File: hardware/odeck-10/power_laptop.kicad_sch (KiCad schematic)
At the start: 0 parts

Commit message: Draft power sheets (input, laptop output, rails) and BOM stock audit
- power_input: TPS26750/TPD4S480 EPR sink, LM74800 PD-in and barrel paths
  (reverse/OV/UV), hardware PD-in priority, EXT_PWR_PRESENT, INA237 VIN monitor
- power_laptop: LM51770 buck-boost 5-28 V x 5 A with VSEL-only voltage steps,
  gated source switch, interlocked bus-power sink, latched 30.8 V OVP, INA226
- power_rails: LM5148 5 V/8 A with ideal-diode backfeed blocking, TPS62933
  3.3 V and 1.15 V, INA226
- tools/bom_check.py: JLC-stock-only audit (>=5); all 116 parts pass
- schgen fixes: multi-line notes, PWR_FLAG skipped in verify, import --force
- docs: design notes per sheet, I2C map, cross-sheet integration items

Co-Authored-By: Claude Opus 5.5 <noreply@anthropic.com>
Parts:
- added C201, C202, C203, C204: 4.7u/100V, Capacitor_SMD:C_1210_3225Metric, symbol Device:C
- added C205: 47u/100V, Capacitor_SMD:CP_Elec_10x10, symbol Device:C_Polarized
- added C206, C207, C208, C209, C210, C211, C233: 10u/50V, Capacitor_SMD:C_1210_3225Metric, symbol Device:C
- added C212, C213: 100u/35V, Capacitor_SMD:CP_Elec_6.3x7.7, symbol Device:C_Polarized
- added C214, C220, C221, C228, C229, C234, C235, C236, C237: 100n/50V, Capacitor_SMD:C_0603_1608Metric, symbol Device:C
- added C215: 100n/100V, Capacitor_SMD:C_0603_1608Metric, symbol Device:C
- added C216: 1u/100V, Capacitor_SMD:C_0805_2012Metric, symbol Device:C
- added C217, C238: 1u/50V, Capacitor_SMD:C_0603_1608Metric, symbol Device:C
- added C218, C219: 22u, Capacitor_SMD:C_0805_2012Metric, symbol Device:C
- added C222: 100p, Capacitor_SMD:C_0402_1005Metric, symbol Device:C
- added C223: 22n, Capacitor_SMD:C_0402_1005Metric, symbol Device:C
- added C224: 6.8n, Capacitor_SMD:C_0402_1005Metric, symbol Device:C
- added C225: 82p, Capacitor_SMD:C_0402_1005Metric, symbol Device:C
- added C226, C240: 1n, Capacitor_SMD:C_0402_1005Metric, symbol Device:C
- added C227: 4.7u, Capacitor_SMD:C_0603_1608Metric, symbol Device:C
- added C230: 22n/50V, Capacitor_SMD:C_0603_1608Metric, symbol Device:C
- added C231, C232, C243: 100n, Capacitor_SMD:C_0402_1005Metric, symbol Device:C
- added C239: 3.3n, Capacitor_SMD:C_0402_1005Metric, symbol Device:C
- added C241: 10u, Capacitor_SMD:C_0805_2012Metric, symbol Device:C
- added C242: 470p, Capacitor_SMD:C_0402_1005Metric, symbol Device:C
- added D201: BZT52C5V1, Diode_SMD:D_SOD-123, symbol Device:D_Zener
- added D202: BAT54A, Package_TO_SOT_SMD:SOT-23, symbol Diode:BAT54A
- added D203: BAV70, Package_TO_SOT_SMD:SOT-23, symbol Diode:BAV70
- added D204: 1N4148W, Diode_SMD:D_SOD-123, symbol Device:D
- added L201: 10u, odeck:IND-SMD_L11.3-W10.0_XAL1010-332ME, symbol odeck:XAL1010-103MED
- added Q201, Q202: BSC0805LS, odeck:PG-TDSON-8_L5.2-W5.9-P1.27-LS6.2-BL-EP, symbol odeck:BSC0805LS
- added Q203, Q204, Q215: CSD18543Q3A, odeck:VSONP-8_L3.1-W3.1-P0.65-LS3.5-BL, symbol odeck:CSD18543Q3A
- added Q205, Q206, Q207, Q208, Q209, Q210, Q211, Q216, Q217, Q218: AO3400A, Package_TO_SOT_SMD:SOT-23, symbol Transistor_FET:AO3400A
- added Q212: 2N7002, Package_TO_SOT_SMD:SOT-23, symbol Transistor_FET:2N7002
- added Q213, Q214: BSC040N08NS5, odeck:PG-TDSON-8_L5.9-W5.1-P1.27-LS6.2-BL, symbol odeck:BSC040N08NS5
- added R201: 4m, Resistor_SMD:R_2512_6332Metric, symbol Device:R
- added R202: 8m, Resistor_SMD:R_2512_6332Metric, symbol Device:R
- added R203, R204, R205, R206, R217, R218: 0, Resistor_SMD:R_0402_1005Metric, symbol Device:R
- added R207: 200k, Resistor_SMD:R_0805_2012Metric, symbol Device:R
- added R208: 43k, Resistor_SMD:R_0402_1005Metric, symbol Device:R
- added R209: 10, Resistor_SMD:R_0603_1608Metric, symbol Device:R
- added R210, R211: 10, Resistor_SMD:R_0402_1005Metric, symbol Device:R
- added R212: 86.6k, Resistor_SMD:R_0402_1005Metric, symbol Device:R
- added R213, R220, R225, R228, R231, R232, R238, R240, R243: 100k, Resistor_SMD:R_0402_1005Metric, symbol Device:R
- added R214: 6.49k, Resistor_SMD:R_0402_1005Metric, symbol Device:R
- added R215: 62k, Resistor_SMD:R_0402_1005Metric, symbol Device:R
- added R216, R219, R236, R239, R247, R249, R253, R255: 10k, Resistor_SMD:R_0402_1005Metric, symbol Device:R
- added R221, R223: 24.3k, Resistor_SMD:R_0402_1005Metric, symbol Device:R
- added R222: 1.5k, Resistor_SMD:R_0402_1005Metric, symbol Device:R
- added R224, R227, R230, R248: 1k, Resistor_SMD:R_0402_1005Metric, symbol Device:R
- added R226: 8.66k, Resistor_SMD:R_0402_1005Metric, symbol Device:R
- added R229: 5.23k, Resistor_SMD:R_0402_1005Metric, symbol Device:R
- added R233: 470k, Resistor_SMD:R_0805_2012Metric, symbol Device:R
- added R234: 150, Resistor_SMD:R_2512_6332Metric, symbol Device:R
- added R235: 255k, Resistor_SMD:R_0402_1005Metric, symbol Device:R
- added R237: 100, Resistor_SMD:R_0402_1005Metric, symbol Device:R
- added R241: 5m, Resistor_SMD:R_2512_6332Metric, symbol Device:R
- added R242: 422k, Resistor_SMD:R_0402_1005Metric, symbol Device:R
- added R244: 121k, Resistor_SMD:R_0402_1005Metric, symbol Device:R
- added R245, R250, R252: 47k, Resistor_SMD:R_0402_1005Metric, symbol Device:R
- added R246: 40.2k, Resistor_SMD:R_0402_1005Metric, symbol Device:R
- added R251: 1.1M, Resistor_SMD:R_0402_1005Metric, symbol Device:R
- added R254: 4.7k, Resistor_SMD:R_0402_1005Metric, symbol Device:R
- added U201: LM51770, odeck:HTSSOP-38_L9.7-W4.4-P0.50-LS6.4-BL-EP, symbol odeck:LM51770DCPR
- added U202: LM74800-Q1, odeck:WSON-12_L3.0-W3.0-P0.50-TL-EP-2, symbol odeck:LM74800QDRRRQ1
- added U203: SN74LVC1G11, Package_TO_SOT_SMD:SOT-23-6, symbol 74xGxx:74LVC1G11
- added U204: INA226, odeck:MSOP-10_L3.0-W3.0-P0.50-LS5.0-BL, symbol odeck:INA226AIDGSR
- added U205: LM74502, odeck:SOT-23-8_L2.9-W1.6-P0.65-LS2.8-BL, symbol odeck:LM74502DDFR
- added U206: TPS259470A, odeck:VQFN-10_L2.0-W2.0-P0.45-TL, symbol odeck:TPS259470ARPWR
- added U207: TLV3011, odeck:SOT-23-6_L2.9-W1.6-P0.95-LS2.8-BR, symbol odeck:TLV3011AIDBVR
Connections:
- new net +3V3: C231.1, C232.1, C243.1, R219.2, R239.2, R255.2, U203.5 (VCC), U204.1 (A1), U204.6 (VS+), U207.6 (VCC)
- new net +5V: C241.1, U206.6 (OUT)
- new net BB_BIAS: C217.1, R209.2, U201.1 (BIAS)
- new net BB_CFG: R214.1, U201.13 (CFG)
- new net BB_COMP: C225.1, R215.1, U201.18 (COMP)
- new net BB_COMPZ: C224.1, R215.2
- new net BB_CSA: C222.1, R210.2, U201.37 (CSA)
- new net BB_CSB: C222.2, R211.2, U201.38 (CSB)
- new net BB_DIS: Q212.3 (D), R234.2
- new net BB_EN: Q209.3 (D), R207.2, R208.1, U201.4 (EN/UVLO)
- new net BB_ENKILL: D201.1 (K), Q208.1 (G), Q209.1 (G), Q210.3 (D), Q212.1 (G), R233.2
- new net BB_ENS: Q210.2 (S), Q211.3 (D)
- new net BB_FB: R220.2, R221.1, R222.1, U201.19 (FB)
- new net BB_FBM: C227.1, R222.2, R223.1, R226.1, R229.1
- new net BB_G1: Q201.4 (G), R203.2
- new net BB_G2: Q202.4 (G), R204.2
- new net BB_G3: Q203.4 (G), R205.2
- new net BB_G4: Q204.4 (G), R206.2
- new net BB_HB1: C220.1, U201.35 (HB1)
- new net BB_HB2: C221.1, U201.26 (HB2)
- new net BB_HO1: R203.1, U201.34 (HO1)
- new net BB_HO2: R206.1, U201.27 (HO2)
- new net BB_IMON: R216.1, U201.6 (IMONOUT)
- new net BB_IMONZ: C226.1, R216.2
- new net BB_LO1: R204.1, U201.32 (LO1)
- new net BB_LO2: R205.1, U201.29 (LO2)
- new net BB_LS: L201.1, R201.2, R211.1
- new net BB_MODE: R217.1, R218.1, U201.12 (MODE)
- new net BB_PSO: C206.1, C207.1, C208.1, C209.1, Q204.5 (D), Q204.6 (D), Q204.7 (D), Q204.8 (D), Q204.9 (D), R202.1, U201.23 (ISNSP)
- new net BB_RT: R212.1, U201.15 (RT)
- new net BB_SLOPE: R213.1, U201.14 (SLOPE)
- new net BB_SS: C223.1, U201.16 (SS/ATRK)
- new net BB_SW1: C220.2, Q201.1 (S), Q201.2 (S), Q201.3 (S), Q202.5 (D), Q202.6 (D), Q202.7 (D), Q202.8 (D), Q202.9 (EP), R201.1, R210.1, U201.36 (SW1)
- new net BB_SW2: C221.2, L201.2, Q203.5 (D), Q203.6 (D), Q203.7 (D), Q203.8 (D), Q203.9 (D), Q204.1 (S), Q204.2 (S), Q204.3 (S), U201.25 (SW2)
- new net BB_VCC: C218.1, C219.1, R218.2, U201.11 (SYNC), U201.31 (VCC)
- new net BB_VS0D: Q205.3 (D), R223.2
- new net BB_VS0G: Q205.1 (G), R224.2
- new net BB_VS1D: Q206.3 (D), R226.2
- new net BB_VS1G: Q206.1 (G), R227.2
- new net BB_VS2D: Q207.3 (D), R229.2
- new net BB_VS2G: Q207.1 (G), R230.2
- new net EXT_PWR_PRESENT: Q216.1 (G), U203.3
- new net GND: C201.2, C202.2, C203.2, C204.2, C205.2, C206.2, C207.2, C208.2, C209.2, C210.2, C211.2, C212.2, C213.2, C214.2, C215.2, C216.2, C217.2, C218.2, C219.2, C223.2, C224.2, C225.2, C226.2, C227.2, C228.2, C230.2, C231.2, C232.2, C233.2, C234.2, C235.2, C236.2, C238.2, C239.2, C240.2, C241.2, C242.2, C243.2, D201.2 (A), Q202.1 (S), Q202.2 (S), Q202.3 (S), Q203.1 (S), Q203.2 (S), Q203.3 (S), Q205.2 (S), Q206.2 (S), Q207.2 (S), Q208.2 (S), Q209.2 (S), Q211.2 (S), Q212.2 (S), Q216.2 (S), Q217.2 (S), Q218.2 (S), R208.2, R212.2, R213.2, R214.2, R217.2, R221.2, R225.2, R228.2, R231.2, R232.2, R236.2, R238.2, R240.2, R243.2, R245.2, R247.2, R248.2, R250.2, R252.2, U201.10 (DTRK), U201.17 (AGND), U201.30 (PGND), U201.39 (EP), U202.7 (GND), U203.2 (GND), U204.2 (A0), U204.7 (GND), U205.2 (GND), U206.8 (GND), U207.2 (GND)
- new net I2C_SYS_SCL: U204.5 (SCL)
- new net I2C_SYS_SDA: U204.4 (SDA)
- new net LAPTOP_OVP_N: D202.2, Q211.1 (G), Q218.3 (D), R255.1
- new net LAPTOP_SNK_EN: R249.1
- new net LAPTOP_SRC_EN: R240.1, U203.1
- new net OVP_DIV: C242.1, R251.2, R252.1, R254.2, U207.3 (IN+)
- new net OVP_FB: D204.1 (K), R254.1
- new net OVP_REF: U207.4 (IN-), U207.5 (REF)
- new net OVP_TOP: D203.3 (K), R251.1
- new net OVP_TRIP: D204.2 (A), Q218.1 (G), R253.1, U207.1 (OUT)
- new net SNK_DVDT: C239.1, U206.7 (DVDT)
- new net SNK_GATE: Q215.4 (G), U205.6 (GATE)
- new net SNK_ILM: R248.1, U206.9 (ILM)
- new net SNK_ITIMER: C240.1, U206.10 (ITIMER)
- new net SNK_MID: C238.1, Q215.1 (S), Q215.2 (S), Q215.3 (S), R244.1, R246.1, U205.8 (SRC), U206.5 (IN)
- new net SNK_ON: Q216.3 (D), Q217.3 (D), R249.2, R250.1, U205.1 (EN/UVLO)
- new net SNK_OV: R242.2, R243.1, U205.7 (OV)
- new net SNK_OVLO: R246.2, R247.1, U206.2 (OVLO/OVCSEL)
- new net SNK_UV: R244.2, R245.1, U206.1 (EN/UVLO)
- new net SNK_VCAP: C237.1, U205.4 (VCAP)
- new net SRC_CAP: C229.1, U202.11 (CAP)
- new net SRC_DGATE: Q213.4 (G), U202.1 (DGATE)
- new net SRC_DVDT: C230.1, R237.2
- new net SRC_HGATE: Q214.4 (G), R237.1, U202.8 (HGATE)
- new net SRC_MID: C228.1, C229.2, Q213.5 (D), Q213.6 (D), Q213.7 (D), Q213.8 (D), Q214.5 (D), Q214.6 (D), Q214.7 (D), Q214.8 (D), U202.10 (VS), U202.12 (C)
- new net SRC_ON: Q217.1 (G), R238.1, U202.6 (EN/UVLO), U203.4
- new net SRC_OV: R235.2, R236.1, U202.5 (OV)
- new net SRC_OVT: R235.1, U202.4 (SW)
- new net SRC_PGOK: D202.3, R239.1, U203.6
- new net VBB_EN: Q210.1 (G), R232.1, R253.2
- new net VBB_OUT: C210.1, C211.1, C212.1, C213.1, C214.1, D203.2 (A), Q213.1 (S), Q213.2 (S), Q213.3 (S), R202.2, R209.1, R220.1, R234.1, U201.20 (VOUT), U201.22 (ISNSN), U202.2 (A)
- new net VBB_PG: D202.1, Q208.3 (D), R219.1, U201.7 (nFLT)
- new net VBB_VSEL0: R224.1, R225.1
- new net VBB_VSEL1: R227.1, R228.1
- new net VBB_VSEL2: R230.1, R231.1
- new net VBUS_LAPTOP: C233.1, C234.1, D203.1 (A), R241.2, U202.3 (VSNS), U204.8 (VBUS), U204.9 (VIN-)
- new net VBUS_LSW: C235.1, C236.1, C237.2, Q214.1 (S), Q214.2 (S), Q214.3 (S), Q215.5 (D), Q215.6 (D), Q215.7 (D), Q215.8 (D), Q215.9 (D), R241.1, R242.1, U202.9 (OUT), U204.10 (VIN+), U205.5 (VS)
- new net VIN: C201.1, C202.1, C203.1, C204.1, C205.1, C215.1, C216.1, Q201.5 (D), Q201.6 (D), Q201.7 (D), Q201.8 (D), Q201.9 (EP), R207.1, R233.1, U201.3 (VIN)
- no-connect marks 0 -> 13
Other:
- note added: "1. LM51770 4-SWITCH BUCK-BOOST POWER STAGE VIN 9-50 V -> VBB_OUT 5.1/9/15/20/28 V, 5 A (140 W) fsw = 347 kHz (RT 86.6k). L = Coilcraft XAL1010-103 10 uH (Isat 17.5 A, 14.75 mOhm max). Ripple: 3.4 A p-p worst (48 V -> 28 V buck), 2.0 A (14 V -> 28 V boost). Input half-bridge: 2x BSC0805LS (100 V, 7.7 mOhm @4.5 V, Qg 16 nC). Output: 2x CSD18543Q3A (60 V, 12 mOhm). Peak current sense RCS = 4 mOhm (W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"
- note added: "2. LM51770 CONTROLLER BIAS from VBB_OUT (10 R/1 uF): VCC LDO runs from min(VIN, VBB_OUT) above 6.5 V -> less LDO loss at 48 V in. EN/UVLO: 200k/43k from VIN -> on at 8.1 V, off at 6.8 V (5 uA hysteresis current). Q pulls EN/UVLO low unless VBB_EN AND LAPTOP_OVP_N (see section 3). CFG 6.49k = R2D #7: spread spectrum ON, hiccup ON, PSM entry 10 %, average current LIMIT on ISNS. SYNC = VCC (positive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"
- note added: "3. OUTPUT VOLTAGE SELECT (PMG1 GPIOs only; RP2350 has no path here) VOUT = 1 V x (1 + Rtop x Gfb). Rtop 100k, Rbot 24.3k -> 5.115 V with all VSEL low (default, no firmware). Switched branches hang off node BB_FBM, which connects to FB through Rs = 1.5k and is held by Cm = 4.7 uF: any VSEL change (even several bits at once) moves the FB current as ONE first-order exponential, tau = Cm x (Rs || bra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"
- note added: "4. LAPTOP SOURCE SWITCH VBB_OUT -> VBUS_LSW -> 5 mOhm -> VBUS_LAPTOP LM74800-Q1: Q (DGATE) = ideal diode (blocks laptop -> VBB_OUT in < 1 us), Q (HGATE) = on/off, common drain, 2x BSC040N08NS5 (80 V, 4 mOhm @10 V): 5 A -> 0.26 W total. HARDWARE ENABLE: SRC_ON = LAPTOP_SRC_EN AND EXT_PWR_PRESENT AND (VBB_PG AND LAPTOP_OVP_N) 74LVC1G11 3-input AND; VBB_PG and LAPTOP_OVP_N (both open-drain, 10k pull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"
- note added: "5. VBUS_LAPTOP MONITOR + CAPACITANCE INA226 on I2C_SYS at 0x44 (A1 = VS, A0 = GND). Shunt 5 mOhm (WSL2512): 5 A -> 25 mV of +-81.92 mV, 0.125 W. Bidirectional: + = sourcing to laptop, - = bus-powered sink. CURRENT_LSB 0.5 mA -> CAL = 2048. VBUS pin on the connector side (36 V max > 32.6 V backstop). Kelvin-route IN+/IN-. ALERT unused. Capacitance on the connector side (VBUS_LAPTOP + VBUS_LSW, no 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"
- note added: "6. BUS-POWER SINK SWITCH VBUS_LSW -> SNK_MID -> +5V (only without external power) Stage 1, 60 V blocking: CSD18543Q3A driven by LM74502 (charge pump, 3.2-65 V). Off -> blocks up to 60 V (VBUS is 28 V when we source); body diode points back to VBUS, reverse handled by stage 2. OV cut-off 422k/100k -> 6.5 V (6.1-6.9 V), 1 us: a >5 V contract can never reach +5V. Stage 2, TPS259470A eFuse (28 V abs)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"
- note added: "7. INDEPENDENT VBUS OVP (latched) -> LAPTOP_OVP_N Senses max(VBUS_LAPTOP, VBB_OUT) through BAV70 (100 V): also catches a run-away buck-boost before the source switch closes. 1.1M/47k + 0.45 V diode: trip = 1.242 x 24.4 + 0.45 = 30.8 V (29.6-32.0 V incl. 1 % ref, 15 mV offset, 1 % R) > 28.7 V max regulation; 470 pF -> 21 us filter. TLV3011 (open-drain, internal 1.242 V ref): output pulled up to VB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"
- note removed: "TODO — planned contents: LM51770 buck-boost 9-48V -> 5/9/15/20/28V x5A, voltage steps via PMG1 GPIO feedback switching, back-to-back source switch to laptop VBUS (enable = ext power AND PG), independent hardware OVP (~30V)."
- title: odeck-10 — Laptop power out -> odeck-10 — Laptop power (buck-boost, source/sink switches, OVP)

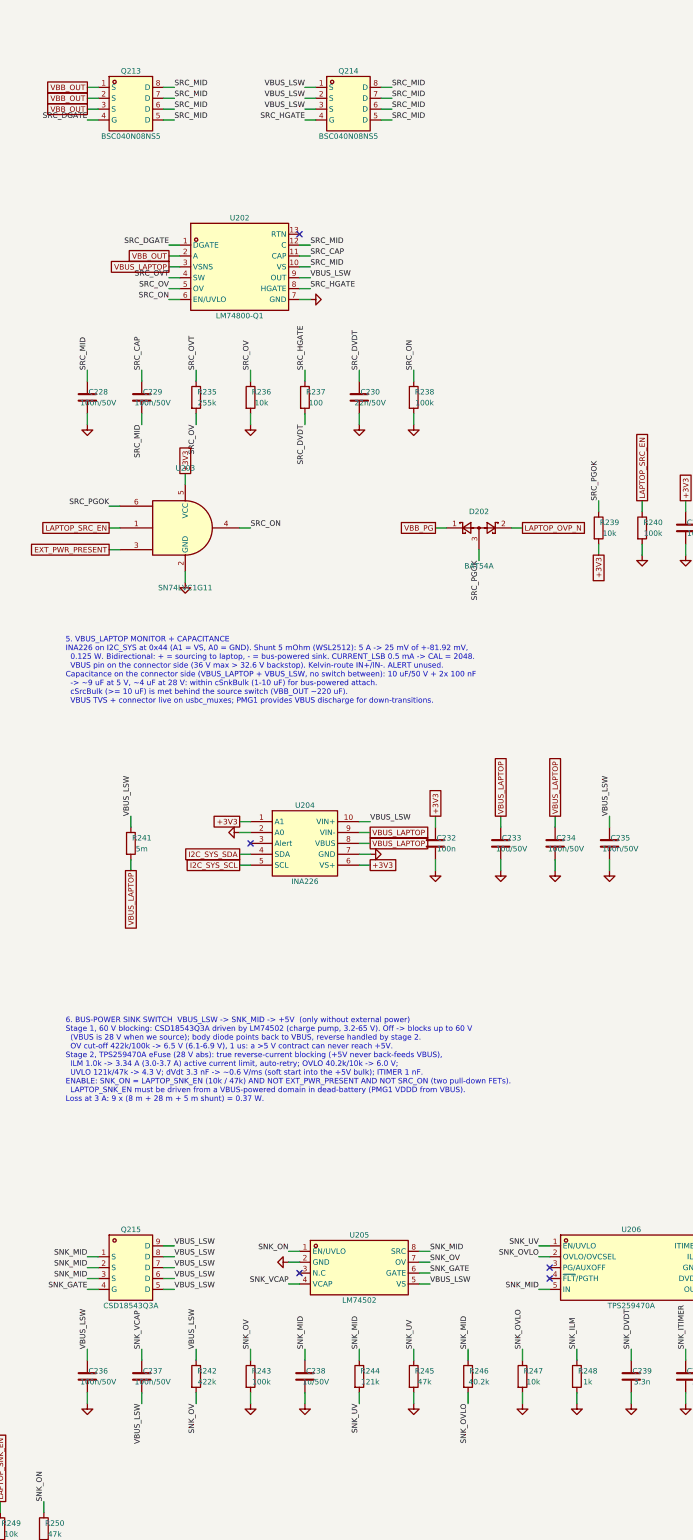
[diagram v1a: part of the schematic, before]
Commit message: Draft data-path sheets: PD controller, USB-C muxes/DP, USB hub
- pd_pmg1: PMG1-S3 (CYPM1321, dead-battery Rd) dual-port: laptop EPR source +
  DP UFP_D, downstream 5 V/3 A + DP DFP_D, HPD relay, VBUS-powered cold start,
  I2C 0x42, SWD/reset via cuttable jumpers
- usbc_muxes: laptop + downstream USB-C, TUSB1064/TUSB1046 in GPIO mode,
  TPD4S480 (EPR) / TPD6S300 CC protection, 10G-rated ESD, AC coupling
- usb_hub: USB7206C port map, SMBus-optional boot, reset gated by RAILS_PG,
  BC1.2 on USB-A ports, hub-TX AC caps
- schgen: in_bom option; nets: VBUS_LSW, PMG1_VDDD, hub/mux/CC links
- import_lcsc.sh: guard against overwriting other parts' footprints
- 137 parts, all JLC stock >= 5

Co-Authored-By: Claude Opus 5.5 <noreply@anthropic.com>
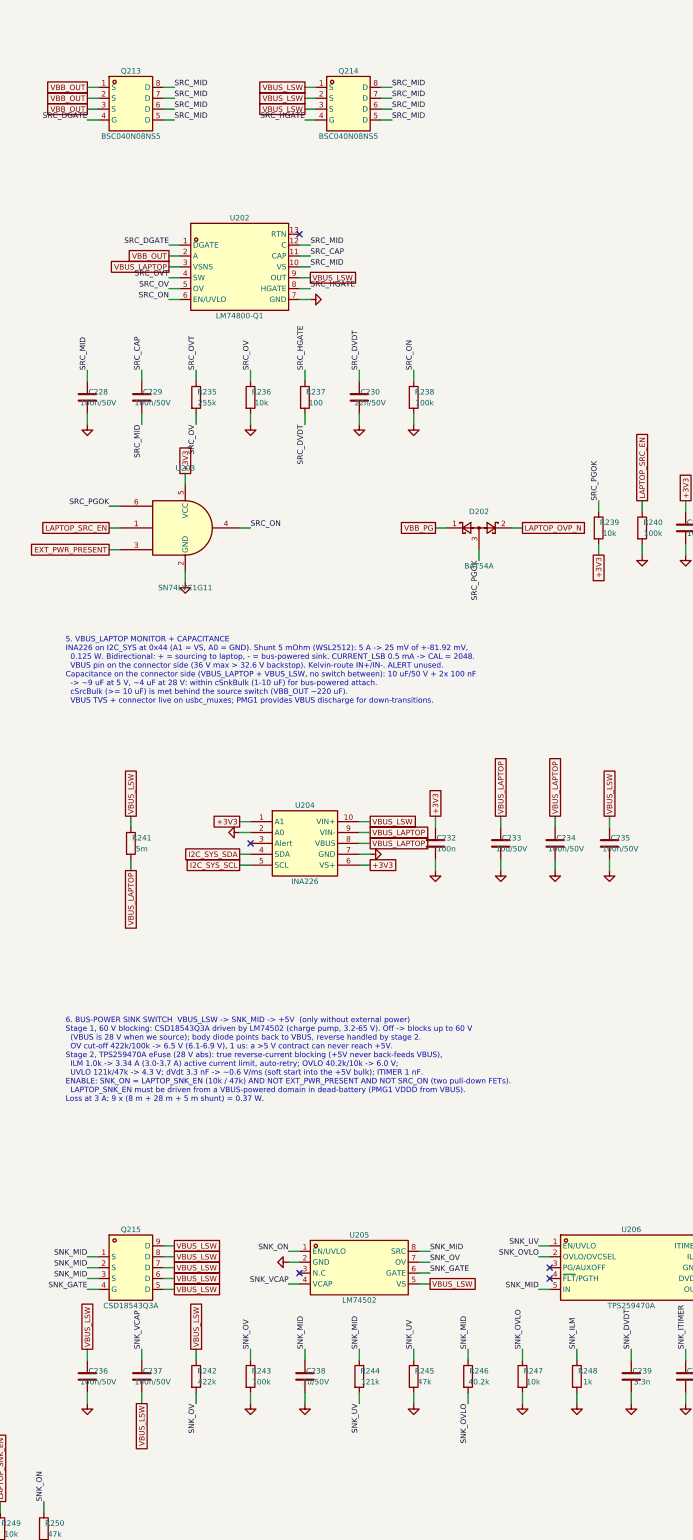
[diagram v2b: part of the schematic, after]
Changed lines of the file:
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@@
 		)
 	)
-	(label "VBUS_LSW"
+	(global_label "VBUS_LSW"
+		(shape passive)
 		(at 462.28 62.23 180)
+		(fields_autoplaced yes)
 		(effects
 			(font
 				(size 1.27 1.27)
 			)
-			(justify right bottom)
+			(justify right)
+		)
+		(property "Intersheetrefs" "${INTERSHEET_REFS}"
+			(at 462.28 62.23 0)
+			(effects
+				(font
+					(size 1.27 1.27)
+				)
+				(hide yes)
+			)
 		)
 	)
@@
 		)
 	)
-	(label "VBUS_LSW"
+	(global_label "VBUS_LSW"
+		(shape passive)
 		(at 462.28 64.77 180)
+		(fields_autoplaced yes)
 		(effects
 			(font
 				(size 1.27 1.27)
 			)
-			(justify right bottom)
+			(justify right)
+		)
+		(property "Intersheetrefs" "${INTERSHEET_REFS}"
+			(at 462.28 64.77 0)
+			(effects
+				(font
+					(size 1.27 1.27)
+				)
+				(hide yes)
+			)
 		)
 	)
@@
 		)
 	)
-	(label "VBUS_LSW"
+	(global_label "VBUS_LSW"
+		(shape passive)
 		(at 462.28 67.31 180)
+		(fields_autoplaced yes)
 		(effects
 			(font
 				(size 1.27 1.27)
 			)
-			(justify right bottom)
+			(justify right)
+		)
+		(property "Intersheetrefs" "${INTERSHEET_REFS}"
+			(at 462.28 67.31 0)
+			(effects
+				(font
+					(size 1.27 1.27)
+				)
+				(hide yes)
+			)
 		)
 	)
@@
 		)
 	)
-	(label "VBUS_LSW"
+	(global_label "VBUS_LSW"
+		(shape passive)
 		(at 463.55 106.68 0)
+		(fields_autoplaced yes)
 		(effects
 			(font
 				(size 1.27 1.27)
 			)
-			(justify left bottom)
+			(justify left)
+		)
+		(property "Intersheetrefs" "${INTERSHEET_REFS}"
+			(at 463.55 106.68 0)
+			(effects
+				(font
+					(size 1.27 1.27)
+				)
+				(hide yes)
+			)
 		)
 	)
@@
 		)
 	)
-	(label "VBUS_LSW"
+	(global_label "VBUS_LSW"
+		(shape passive)
 		(at 421.64 232.41 90)
+		(fields_autoplaced yes)
 		(effects
 			(font
 				(size 1.27 1.27)
 			)
-			(justify left bottom)
+			(justify left)
+		)
+		(property "Intersheetrefs" "${INTERSHEET_REFS}"
+			(at 421.64 232.41 0)
+			(effects
+				(font
+					(size 1.27 1.27)
+				)
+				(hide yes)
+			)
 		)
 	)
@@
 		)
 	)
-	(label "VBUS_LSW"
+	(global_label "VBUS_LSW"
+		(shape passive)
 		(at 477.52 233.68 0)
+		(fields_autoplaced yes)
 		(effects
 			(font
 				(size 1.27 1.27)
 			)
-			(justify left bottom)
+			(justify left)
+		)
+		(property "Intersheetrefs" "${INTERSHEET_REFS}"
+			(at 477.52 233.68 0)
+			(effects
+				(font
+					(size 1.27 1.27)
+				)
+				(hide yes)
+			)
 		)
 	)
@@
 		)
 	)
-	(label "VBUS_LSW"
+	(global_label "VBUS_LSW"
+		(shape passive)
 		(at 533.40 232.41 90)
+		(fields_autoplaced yes)
 		(effects
 			(font
 				(size 1.27 1.27)
 			)
-			(justify left bottom)
+			(justify left)
+		)
+		(property "Intersheetrefs" "${INTERSHEET_REFS}"
+			(at 533.40 232.41 0)
+			(effects
+				(font
+					(size 1.27 1.27)
+				)
+				(hide yes)
+			)
 		)
 	)
@@
 		)
 	)
-	(label "VBUS_LSW"
+	(global_label "VBUS_LSW"
+		(shape passive)
 		(at 431.80 342.90 0)
+		(fields_autoplaced yes)
 		(effects
 			(font
 				(size 1.27 1.27)
 			)
-			(justify left bottom)
+			(justify left)
+		)
+		(property "Intersheetrefs" "${INTERSHEET_REFS}"
+			(at 431.80 342.90 0)
+			(effects
+				(font
+					(size 1.27 1.27)
+				)
+				(hide yes)
+			)
 		)
 	)
@@
 		)
 	)
-	(label "VBUS_LSW"
+	(global_label "VBUS_LSW"
+		(shape passive)
 		(at 431.80 340.36 0)
+		(fields_autoplaced yes)
 		(effects
 			(font
 				(size 1.27 1.27)
 			)
-			(justify left bottom)
+			(justify left)
+		)
+		(property "Intersheetrefs" "${INTERSHEET_REFS}"
+			(at 431.80 340.36 0)
+			(effects
+				(font
+					(size 1.27 1.27)
+				)
+				(hide yes)
+			)
 		)
 	)
@@
 		)
 	)
-	(label "VBUS_LSW"
+	(global_label "VBUS_LSW"
+		(shape passive)
 		(at 431.80 337.82 0)
+		(fields_autoplaced yes)
 		(effects
 			(font
 				(size 1.27 1.27)
 			)
-			(justify left bottom)
+			(justify left)
+		)
+		(property "Intersheetrefs" "${INTERSHEET_REFS}"
+			(at 431.80 337.82 0)
+			(effects
+				(font
+					(size 1.27 1.27)
+				)
+				(hide yes)
+			)
 		)
 	)
@@
 		)
 	)
-	(label "VBUS_LSW"
+	(global_label "VBUS_LSW"
+		(shape passive)
 		(at 431.80 335.28 0)
+		(fields_autoplaced yes)
 		(effects
 			(font
 				(size 1.27 1.27)
 			)
-			(justify left bottom)
+			(justify left)
+		)
+		(property "Intersheetrefs" "${INTERSHEET_REFS}"
+			(at 431.80 335.28 0)
+			(effects
+				(font
+					(size 1.27 1.27)
+				)
+				(hide yes)
+			)
 		)
 	)
@@
 		)
 	)
-	(label "VBUS_LSW"
+	(global_label "VBUS_LSW"
+		(shape passive)
 		(at 431.80 332.74 0)
+		(fields_autoplaced yes)
 		(effects
 			(font
 				(size 1.27 1.27)
 			)
-			(justify left bottom)
+			(justify left)
+		)
+		(property "Intersheetrefs" "${INTERSHEET_REFS}"
+			(at 431.80 332.74 0)
+			(effects
+				(font
+					(size 1.27 1.27)
+				)
+				(hide yes)
+			)
 		)
 	)
@@
 		)
 	)
-	(label "VBUS_LSW"
+	(global_label "VBUS_LSW"
+		(shape passive)
 		(at 491.49 341.63 0)
+		(fields_autoplaced yes)
 		(effects
 			(font
 				(size 1.27 1.27)
 			)
-			(justify left bottom)
+			(justify left)
+		)
+		(property "Intersheetrefs" "${INTERSHEET_REFS}"
+			(at 491.49 341.63 0)
+			(effects
+				(font
+					(size 1.27 1.27)
+				)
+				(hide yes)
+			)
 		)
 	)
@@
 		)
 	)
-	(label "VBUS_LSW"
+	(global_label "VBUS_LSW"
+		(shape passive)
 		(at 411.48 356.87 90)
+		(fields_autoplaced yes)
 		(effects
 			(font
 				(size 1.27 1.27)
 			)
-			(justify left bottom)
+			(justify left)
+		)
+		(property "Intersheetrefs" "${INTERSHEET_REFS}"
+			(at 411.48 356.87 0)
+			(effects
+				(font
+					(size 1.27 1.27)
+				)
+				(hide yes)
+			)
 		)
 	)
@@
 		)
 	)
-	(label "VBUS_LSW"
+	(global_label "VBUS_LSW"
+		(shape passive)
 		(at 424.18 369.57 270)
+		(fields_autoplaced yes)
 		(effects
 			(font
 				(size 1.27 1.27)
 			)
-			(justify right bottom)
+			(justify right)
+		)
+		(property "Intersheetrefs" "${INTERSHEET_REFS}"
+			(at 424.18 369.57 0)
+			(effects
+				(font
+					(size 1.27 1.27)
+				)
+				(hide yes)
+			)
 		)
 	)
@@
 		)
 	)
-	(label "VBUS_LSW"
+	(global_label "VBUS_LSW"
+		(shape passive)
 		(at 436.88 356.87 90)
+		(fields_autoplaced yes)
 		(effects
 			(font
 				(size 1.27 1.27)
 			)
-			(justify left bottom)
+			(justify left)
+		)
+		(property "Intersheetrefs" "${INTERSHEET_REFS}"
+			(at 436.88 356.87 0)
+			(effects
+				(font
+					(size 1.27 1.27)
+				)
+				(hide yes)
+			)
 		)
 	)
